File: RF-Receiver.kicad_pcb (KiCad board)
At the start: 2 copper layers, 45 x 46.4 mm, 25 parts, among them J1 U.FL-R-SMT_01_, SW1 Button, U1 ESP32-PICO-D4, U2 SX1280IMLTRT, U3 LDO, Y1 Crystal

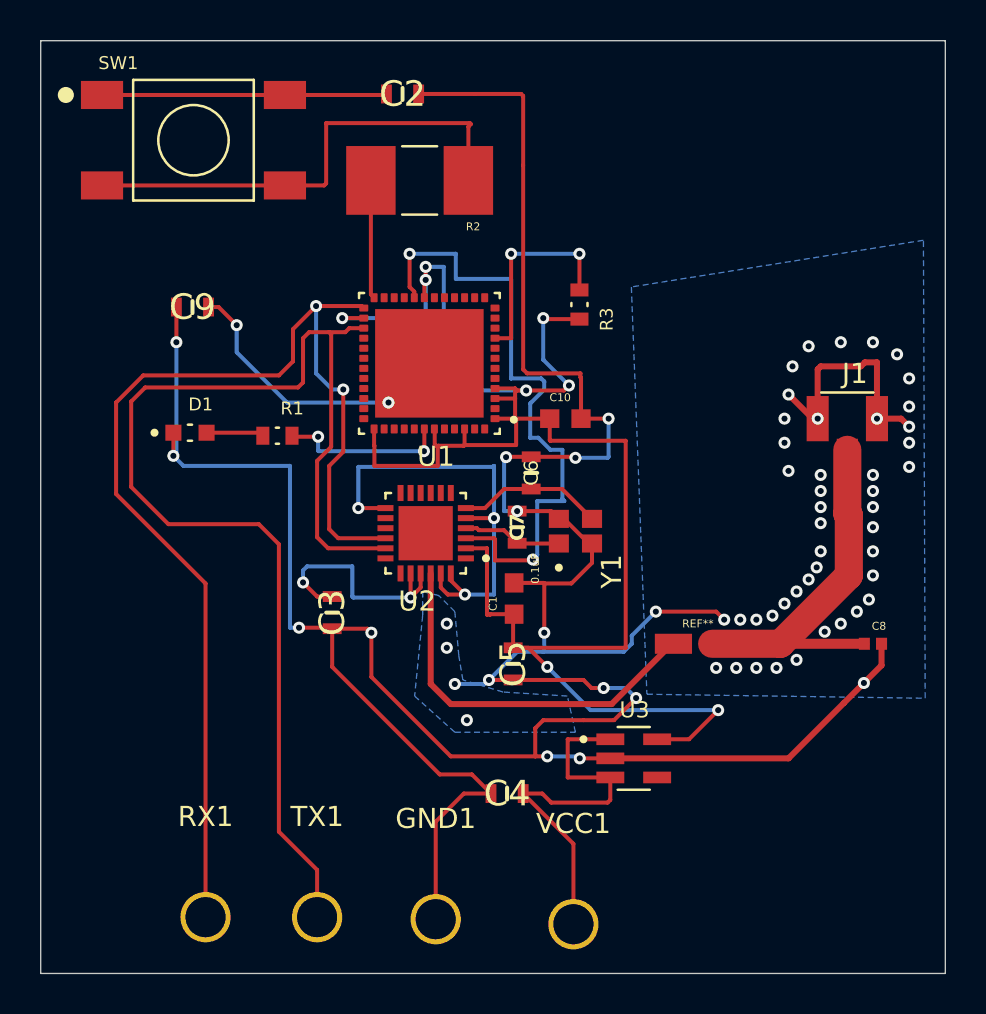
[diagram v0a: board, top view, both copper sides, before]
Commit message: Project Files
Update to board and schematic
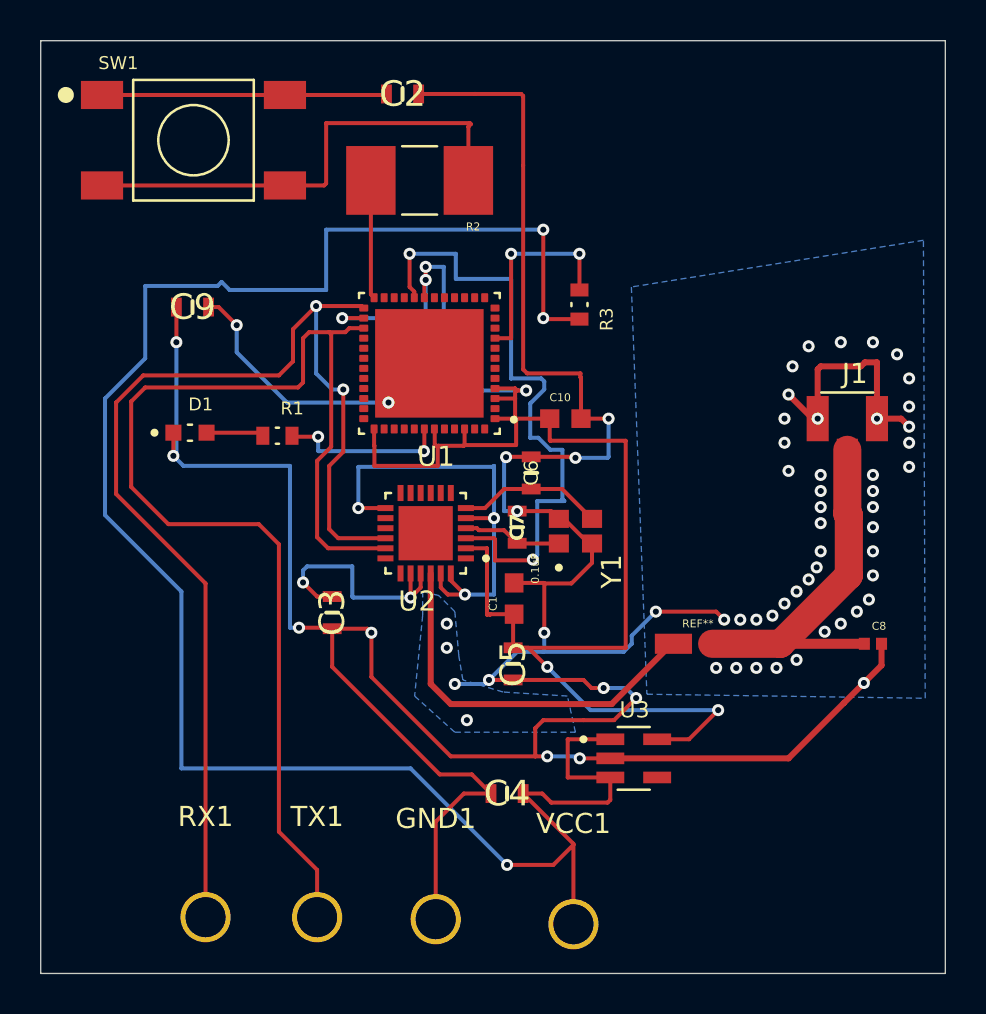
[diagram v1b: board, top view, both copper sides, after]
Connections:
- R3 pad 2: Pico_VDD -> VCC
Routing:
- net VCC: track 19.4 -> 96.9 mm, vias 0 -> 3
- net Pico_VDD: track 90.9 -> 83.0 mm, vias 8 -> 6
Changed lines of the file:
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@@
 			(size 0.65 0.9)
 			(layers "F.Cu" "F.Mask" "F.Paste")
-			(net 11 "Pico_VDD")
+			(net 9 "VCC")
 			(pintype "passive")
 			(solder_mask_margin 0.102)
@@
 	)
 	(segment
+		(start 265 101.65)
+		(end 263.25 101.65)
+		(width 0.2)
+		(layer "F.Cu")
+		(net 9)
+	)
+	(segment
 		(start 266.535 125.565)
 		(end 266.4 125.7)
@@
 	)
 	(segment
+		(start 261.4 128.8)
+		(end 263.7 128.8)
+		(width 0.2)
+		(layer "F.Cu")
+		(net 9)
+	)
+	(segment
 		(start 266.4 125.7)
 		(end 263.6 125.7)
@@
 	)
 	(segment
+		(start 263.2 101.6)
+		(end 263.2 97.2)
+		(width 0.2)
+		(layer "F.Cu")
+		(net 9)
+	)
+	(segment
 		(start 266.535 122.55)
 		(end 264.415 122.55)
@@
 	)
 	(segment
+		(start 263.25 101.65)
+		(end 263.2 101.6)
+		(width 0.2)
+		(layer "F.Cu")
+		(net 9)
+	)
+	(segment
 		(start 264.7 127.75)
-		(end 264.7 131.75)
+		(end 264.7 127.8)
+		(width 0.2)
+		(layer "F.Cu")
+		(net 9)
+	)
+	(segment
+		(start 263.7 128.8)
+		(end 264.7 127.8)
 		(width 0.2)
 		(layer "F.Cu")
@@
 	)
 	(segment
+		(start 264.7 127.8)
+		(end 264.7 131.75)
+		(width 0.2)
+		(layer "F.Cu")
+		(net 9)
+	)
+	(via
+		(at 263.2 101.6)
+		(size 0.6)
+		(drill 0.3)
+		(layers "F.Cu" "B.Cu")
+		(net 9)
+	)
+	(via
+		(at 261.4 128.8)
+		(size 0.6)
+		(drill 0.3)
+		(layers "F.Cu" "B.Cu")
+		(net 9)
+	)
+	(via
+		(at 263.2 97.2)
+		(size 0.6)
+		(drill 0.3)
+		(layers "F.Cu" "B.Cu")
+		(net 9)
+	)
+	(segment
+		(start 252.4 97.2)
+		(end 252.4 100.2)
+		(width 0.2)
+		(layer "B.Cu")
+		(net 9)
+	)
+	(segment
+		(start 243.4 103.6)
+		(end 241.4 105.6)
+		(width 0.2)
+		(layer "B.Cu")
+		(net 9)
+	)
+	(segment
+		(start 252.4 100.2)
+		(end 247.6 100.2)
+		(width 0.2)
+		(layer "B.Cu")
+		(net 9)
+	)
+	(segment
+		(start 243.4 100)
+		(end 243.4 103.6)
+		(width 0.2)
+		(layer "B.Cu")
+		(net 9)
+	)
+	(segment
+		(start 263.2 97.2)
+		(end 252.4 97.2)
+		(width 0.2)
+		(layer "B.Cu")
+		(net 9)
+	)
+	(segment
+		(start 245.2 115.2)
+		(end 245.2 124)
+		(width 0.2)
+		(layer "B.Cu")
+		(net 9)
+	)
+	(segment
+		(start 241.4 111.4)
+		(end 245.2 115.2)
+		(width 0.2)
+		(layer "B.Cu")
+		(net 9)
+	)
+	(segment
+		(start 241.4 105.6)
+		(end 241.4 111.4)
+		(width 0.2)
+		(layer "B.Cu")
+		(net 9)
+	)
+	(segment
+		(start 247.6 100.2)
+		(end 247.2 99.8)
+		(width 0.2)
+		(layer "B.Cu")
+		(net 9)
+	)
+	(segment
+		(start 245.2 124)
+		(end 256.6 124)
+		(width 0.2)
+		(layer "B.Cu")
+		(net 9)
+	)
+	(segment
+		(start 247 100)
+		(end 243.4 100)
+		(width 0.2)
+		(layer "B.Cu")
+		(net 9)
+	)
+	(segment
+		(start 256.6 124)
+		(end 261.4 128.8)
+		(width 0.2)
+		(layer "B.Cu")
+		(net 9)
+	)
+	(segment
+		(start 247.2 99.8)
+		(end 247 100)
+		(width 0.2)
+		(layer "B.Cu")
+		(net 9)
+	)
+	(segment
 		(start 258 107.95)
 		(end 259.25 107.95)
@@
 	)
 	(segment
-		(start 265 101.65)
-		(end 263.25 101.65)
-		(width 0.2)
-		(layer "F.Cu")
-		(net 11)
-	)
-	(segment
 		(start 267.3 118)
 		(end 267.3 107.7)
@@
 	)
 	(segment
-		(start 263.25 101.65)
-		(end 263.2 101.6)
-		(width 0.2)
-		(layer "F.Cu")
-		(net 11)
-	)
-	(segment
 		(start 261.8 105.6)
 		(end 261.8 106.6)
@@
 	)
 	(segment
-		(start 264.478 104.95)
-		(end 264.228 105.2)
-		(width 0.2)
-		(layer "F.Cu")
-		(net 11)
-	)
-	(segment
 		(start 260.4 116.35)
 		(end 260.55 116.35)
@@
 	)
 	(segment
-		(start 264.228 105.2)
-		(end 262.35 105.2)
-		(width 0.2)
-		(layer "F.Cu")
-		(net 11)
-	)
-	(segment
 		(start 259.285 107.915)
 		(end 261.835 107.915)
@@
 	)
 	(via
-		(at 263.2 101.6)
-		(size 0.6)
-		(drill 0.3)
-		(layers "F.Cu" "B.Cu")
-		(net 11)
-	)
-	(via
 		(at 257.35 99.7)
 		(size 0.6)
@@
 	)
 	(via
-		(at 264.478 104.95)
-		(size 0.6)
-		(drill 0.3)
-		(layers "F.Cu" "B.Cu")
-		(net 11)
-	)
-	(via
 		(at 271.9 121.1)
 		(size 0.6)
@@
 	)
 	(segment
-		(start 263.2 101.6)
-		(end 263.2 103.672)
-		(width 0.2)
-		(layer "B.Cu")
-		(net 11)
-	)
-	(segment
 		(start 257.35 100.6)
 		(end 257.35 99.7)
@@
 		(width 0.2)
 		(layer "B.Cu")
-		(net 11)
-	)
-	(segment
-		(start 263.2 103.672)
-		(end 264.478 104.95)
-		(width 0.2)
-		(layer "B.Cu")
